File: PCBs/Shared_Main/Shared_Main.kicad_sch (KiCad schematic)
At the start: 19 parts, among them J1 +5V and GND, J16 Conn_RJ45_Right_To_Left, J3 Encoder inputs B, J4 Encoder inputs A, J5 Analog inputs, J7 Conn_Right_Keypad, J8 Rotary switchs' pin 1, U1 MCP23017_SP, U10 MAX485E, U2 ULN2003A

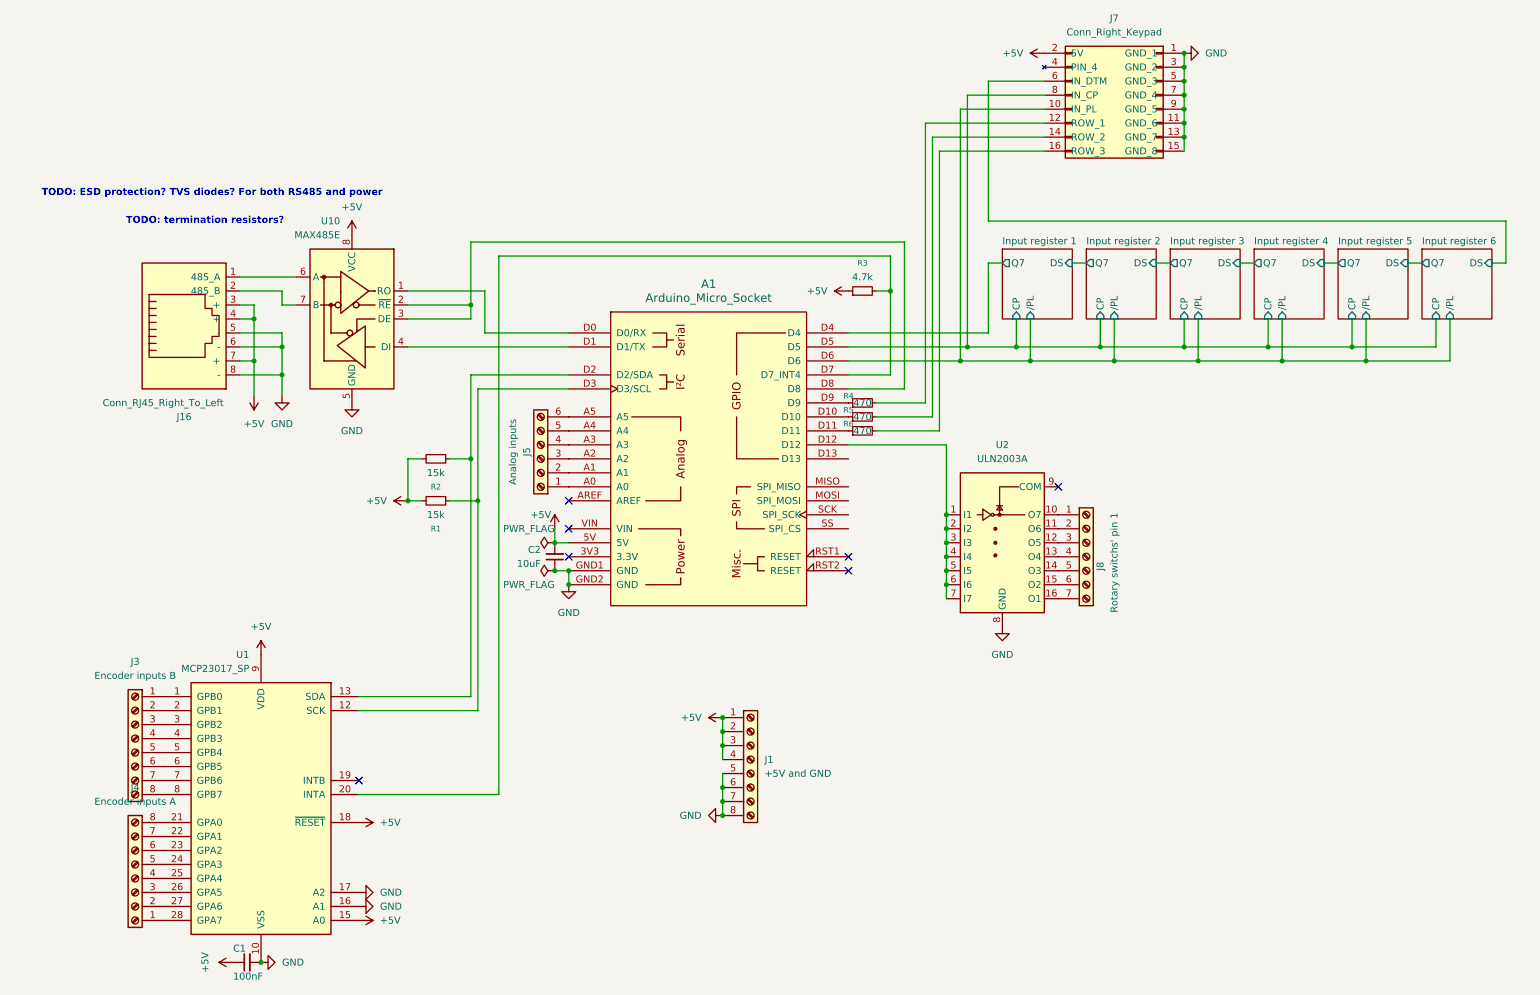
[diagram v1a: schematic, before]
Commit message: Shared main with ESP32-S3-ZERO's, schematic draft
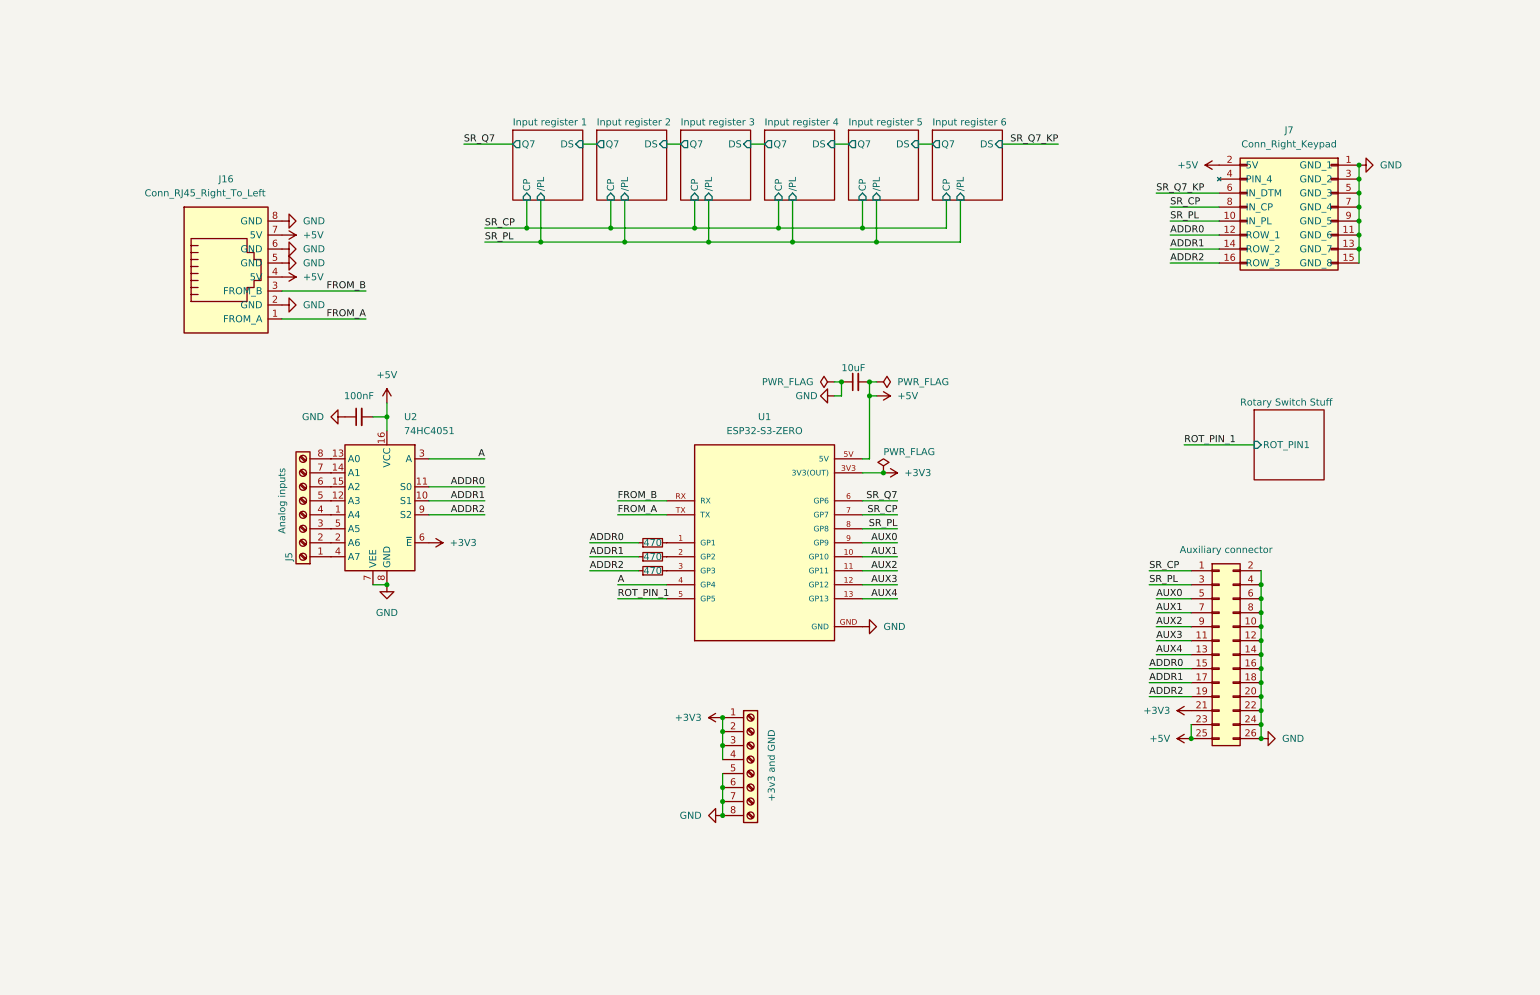
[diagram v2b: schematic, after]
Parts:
- removed A1: Arduino_Micro_Socket, arduino-library:Arduino_Micro_Socket, symbol arduino-library:Arduino_Micro_Socket
- removed J3: Encoder inputs B, TerminalBlock_Phoenix:TerminalBlock_Phoenix_MPT-0,5-8-2.54_1x08_P2.54mm_Horizontal, symbol Connector:Screw_Terminal_01x08
- removed J4: Encoder inputs A, TerminalBlock_Phoenix:TerminalBlock_Phoenix_MPT-0,5-8-2.54_1x08_P2.54mm_Horizontal, symbol Connector:Screw_Terminal_01x08
- removed J8: Rotary switchs' pin 1, TerminalBlock_Phoenix:TerminalBlock_Phoenix_MPT-0,5-7-2.54_1x07_P2.54mm_Horizontal, symbol Connector:Screw_Terminal_01x07
- removed R1, R2: 15k, Resistor_THT:R_Axial_DIN0207_L6.3mm_D2.5mm_P7.62mm_Horizontal, symbol Device:R_Small
- removed R3: 4.7k, Resistor_THT:R_Axial_DIN0207_L6.3mm_D2.5mm_P7.62mm_Horizontal, symbol Device:R_Small
- removed U1: MCP23017_SP, Package_DIP:DIP-28_W7.62mm, symbol Interface_Expansion:MCP23017_SP
- removed U10: MAX485E, Package_DIP:DIP-8_W7.62mm, symbol Interface_UART:MAX485E
- removed U2: ULN2003A, Package_DIP:DIP-16_W7.62mm, symbol Transistor_Array:ULN2003A
- added J3: Auxiliary connector, symbol Connector_Generic:Conn_02x13_Odd_Even
- added U1: ESP32-S3-ZERO, ESP32-S3-ZERO:MODULE_ESP32-S3-ZERO, symbol ESP32-S3-ZERO:ESP32-S3-ZERO
- added U2: 74HC4051, symbol 74xx:74HC4051
- C1: footprint Capacitor_THT:C_Disc_D5.0mm_W2.5mm_P2.50mm -> (none)
- J1: value +5V and GND -> +3v3 and GND
- J5: symbol Connector:Screw_Terminal_01x06 -> Connector:Screw_Terminal_01x08
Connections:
- net +5V: now also C1.2, J3.23 (Pin_23), J3.25 (Pin_25), U1.5V, U2.16 (VCC); no longer C1.1, J1.1 (Pin_1), J1.2 (Pin_2), J1.3 (Pin_3), J1.4 (Pin_4), J16.3 (+)
- net GND: now also C1.1, J16.2 (GND), J3.10 (Pin_10), J3.12 (Pin_12), J3.14 (Pin_14), J3.16 (Pin_16), J3.18 (Pin_18), J3.2 (Pin_2), J3.20 (Pin_20), J3.22 (Pin_22), J3.24 (Pin_24), J3.26 (Pin_26), J3.4 (Pin_4), J3.6 (Pin_6), J3.8 (Pin_8), U1.GND, U2.7 (VEE), U2.8 (GND); no longer C1.2
- net ADDR2: now reaches R6.1
- net ADDR2: now also J7.16 (ROW_3), J3.19 (Pin_19), U2.9 (S2)
- net at R6.2: now also U1.3 (GP3); no longer J7.16 (ROW_3)
- net at R4.2: now also U1.1 (GP1); no longer J7.12 (ROW_1)
- net at R5.2: now also U1.2 (GP2); no longer J7.14 (ROW_2)
- net at J5.1 (Pin_1): now also U2.4 (A7)
- net at J5.2 (Pin_2): now also U2.2 (A6)
- net at J5.3 (Pin_3): now also U2.5 (A5)
- net at J5.4 (Pin_4): now also U2.1 (A4)
- net at J5.5 (Pin_5): now also U2.12 (A3)
- net at J5.6 (Pin_6): now also U2.15 (A2)
- net ADDR1: now reaches R5.1
- net ADDR1: now also J7.14 (ROW_2), J3.17 (Pin_17), U2.10 (S1)
- net ADDR0: now reaches R4.1
- net ADDR0: now also J7.12 (ROW_1), J3.15 (Pin_15), U2.11 (S0)
- net FROM_A: now reaches J16.1 (FROM_A)
- net FROM_A: now also U1.TX
- net Input register 1/CP renamed SR_CP
- net SR_CP: now also J3.1 (Pin_1), U1.7 (GP7)
- net Input register 1//PL renamed SR_PL
- net SR_PL: now also J3.3 (Pin_3), U1.8 (GP8)
- net Input register 6/DS renamed SR_Q7_KP
- new net: J5.7 (Pin_7), U2.14 (A1)
- new net: J5.8 (Pin_8), U2.13 (A0)
- new net +3V3: J1.1 (Pin_1), J1.2 (Pin_2), J1.3 (Pin_3), J1.4 (Pin_4), J3.21 (Pin_21), U1.3V3 (3V3(OUT)), U2.6 (~{E})
- new net A: U1.4 (GP4), U2.3 (A)
- new net AUX0: J3.5 (Pin_5), U1.9 (GP9)
- new net AUX1: J3.7 (Pin_7), U1.10 (GP10)
- new net AUX2: J3.9 (Pin_9), U1.11 (GP11)
- new net AUX3: J3.11 (Pin_11), U1.12 (GP12)
- new net AUX4: J3.13 (Pin_13), U1.13 (GP13)
- new net FROM_B: J16.3 (FROM_B), U1.RX
- new net ROT_PIN_1: U1.5 (GP5)
- new net SR_Q7: U1.6 (GP6)
- no-connect marks 7 -> 0
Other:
- added sheet Rotary Switch Stuff (Rotary_Switch_Stuff.kicad_sch)
- note removed: "TODO: ESD protection? TVS diodes? For both RS485 and power"
- note removed: "TODO: termination resistors?"
- moved on the sheet: J16, J7

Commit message: shared main wip
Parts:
- removed J1: +3v3 and GND, TerminalBlock_Phoenix:TerminalBlock_Phoenix_MPT-0,5-8-2.54_1x08_P2.54mm_Horizontal, symbol Connector:Screw_Terminal_01x08
- removed J3: Auxiliary connector, symbol Connector_Generic:Conn_02x13_Odd_Even
- added J1: Power, TerminalBlock_Phoenix:TerminalBlock_Phoenix_PT-1,5-3-5.0-H_1x03_P5.00mm_Horizontal, symbol Connector:Screw_Terminal_01x03
- added J4: Aux, Connector_PinHeader_2.54mm:PinHeader_1x10_P2.54mm_Vertical, symbol Connector_Generic:Conn_01x10
- C1: footprint (none) -> Capacitor_THT:C_Disc_D5.0mm_W2.5mm_P2.50mm
- J16: value Conn_RJ45_Right_To_Left -> To other side
- J5: footprint TerminalBlock_Phoenix:TerminalBlock_Phoenix_MPT-0,5-6-2.54_1x06_P2.54mm_Horizontal -> TerminalBlock_Phoenix:TerminalBlock_Phoenix_MPT-0,5-8-2.54_1x08_P2.54mm_Horizontal
- J7: value Conn_Right_Keypad -> Keypad
- U2: footprint (none) -> Package_DIP:DIP-16_W7.62mm
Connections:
- net +3V3: now also J1.1 (Pin_1)
- net +5V: now also J1.3 (Pin_3)
- net ADDR0: now also J4.8 (Pin_8)
- net ADDR1: now also J4.9 (Pin_9)
- net ADDR2: now also J4.10 (Pin_10)
- net AUX0: now also J4.3 (Pin_3)
- net AUX1: now also J4.4 (Pin_4)
- net AUX2: now also J4.5 (Pin_5)
- net AUX3: now also J4.6 (Pin_6)
- net AUX4: now also J4.7 (Pin_7)
- net GND: now also J1.2 (Pin_2)
- net SR_CP: now also J4.1 (Pin_1)
- net SR_PL: now also J4.2 (Pin_2)

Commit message: stuff
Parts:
- added H1, H2, H3, H4: M3, MountingHole:MountingHole_3.2mm_M3, symbol Mechanical:MountingHole
- added R2, R3: 100, Resistor_THT:R_Axial_DIN0207_L6.3mm_D2.5mm_P7.62mm_Horizontal, symbol Device:R_Small
- J16: value To other side -> Other unit
- R4, R5, R6: value 470 -> 100
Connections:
- net +3V3: now also C1.2, J7.2 (3v3), U2.16 (VCC)
- net +5V: no longer C1.2, J7.2 (5V), U2.16 (VCC)
- net ADDR0: now also J4.10 (Pin_10), R4.2, U1.1 (GP1); no longer J4.8 (Pin_8), J7.12 (ROW_1), R4.1
- net ADDR1: now also R5.2, U1.2 (GP2); no longer J7.14 (ROW_2), R5.1
- net ADDR2: now also J4.8 (Pin_8), R6.2, U1.3 (GP3); no longer J4.10 (Pin_10), J7.16 (ROW_3), R6.1
- net FROM_A: now also R3.2; no longer J16.1 (FROM_A)
- net FROM_B: now also R2.2; no longer J16.3 (FROM_B)
- new net: J16.1 (FROM_A), R3.1
- new net: J16.3 (FROM_B), R2.1
- new net ADDR0_KP: J7.12 (ROW_1), R4.1
- new net ADDR1_KP: J7.14 (ROW_2), R5.1
- new net ADDR2_KP: J7.16 (ROW_3), R6.1
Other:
- moved on the sheet: U1

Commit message: wip
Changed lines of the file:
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@@
 	(wire
 		(pts
+			(xy 232.41 144.78) (xy 238.76 144.78)
+		)
+		(stroke
+			(width 0)
+			(type default)
+		)
+	)
+	(wire
+		(pts
 			(xy 185.42 54.61) (xy 185.42 62.23)
 		)
@@
 	(wire
 		(pts
-			(xy 238.76 149.86) (xy 232.41 149.86)
-		)
-		(stroke
-			(width 0)
-			(type default)
-		)
-	)
-	(wire
-		(pts
 			(xy 167.64 54.61) (xy 167.64 59.69)
 		)
@@
 	(wire
 		(pts
-			(xy 238.76 144.78) (xy 232.41 144.78)
+			(xy 232.41 149.86) (xy 238.76 149.86)
 		)
 		(stroke
@@
 	)
 	(label "ADDR0"
-		(at 232.41 144.78 0)
+		(at 232.41 149.86 0)
 		(effects
 			(font
@@
 	)
 	(label "ADDR2"
-		(at 232.41 149.86 0)
+		(at 232.41 144.78 0)
 		(effects
 			(font
